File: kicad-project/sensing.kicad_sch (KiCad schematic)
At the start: 10 parts, among them J7 Screw_Terminal_01x04

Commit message: commit anonimo di thimas
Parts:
- added TP4, TP5: TestPoint, TestPoint:TestPoint_Keystone_5005-5009_Compact, symbol Connector:TestPoint
- gave numbers to parts that had none: 1
- renumbered D6 to D8, J7 to J8, R22 to R21, R24 to R22, R25 to R23
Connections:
- net Pan_V_Part: now also TP5.1
- net Shunt+: now also TP4.1
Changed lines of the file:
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@@
+    (stroke (width 0) (type default) (color 0 0 0 0))
+  )
+  (wire (pts (xy 99.06 97.79) (xy 111.76 97.79))
     (stroke (width 0) (type default) (color 0 0 0 0))
   )
@@
   )
   (wire (pts (xy 54.61 60.96) (xy 54.61 63.5))
+    (stroke (width 0) (type default) (color 0 0 0 0))
+  )
+  (wire (pts (xy 99.06 86.36) (xy 107.95 86.36))
     (stroke (width 0) (type default) (color 0 0 0 0))
   )
@@
     (effects (font (size 1.27 1.27)) (justify left bottom))
   )
+  (label "Shunt+" (at 99.06 86.36 0)
+    (effects (font (size 1.27 1.27)) (justify left bottom))
+  )
   (label "Pan_V_Part" (at 109.22 52.07 0)
     (effects (font (size 1.27 1.27)) (justify left bottom))
   )
   (label "Panel OUT -" (at 38.1 95.25 0)
+    (effects (font (size 1.27 1.27)) (justify left bottom))
+  )
+  (label "Pan_V_Part" (at 99.06 97.79 0)
     (effects (font (size 1.27 1.27)) (justify left bottom))
   )
@@
   (symbol (lib_id "Device:Opamp_Dual") (at 129.54 54.61 0) (unit 2)
     (in_bom yes) (on_board yes) (fields_autoplaced)
-    (property "Reference" "U?" (id 0) (at 129.54 44.45 0))
+    (property "Reference" "U5" (id 0) (at 129.54 44.45 0))
     (property "Value" "LM2904B" (id 1) (at 129.54 46.99 0))
     (property "Footprint" "Package_SO:TSSOP-8_4.4x3mm_P0.65mm" (id 2) (at 129.54 54.61 0)
@@
   (symbol (lib_id "power:GND") (at 106.68 60.96 0) (unit 1)
     (in_bom yes) (on_board yes)
-    (property "Reference" "#PWR073" (id 0) (at 106.68 67.31 0)
+    (property "Reference" "#PWR081" (id 0) (at 106.68 67.31 0)
       (effects (font (size 1.27 1.27)) hide)
     )
@@
   (symbol (lib_id "power:+3V3") (at 138.43 36.83 0) (unit 1)
     (in_bom yes) (on_board yes)
-    (property "Reference" "#PWR069" (id 0) (at 138.43 40.64 0)
+    (property "Reference" "#PWR082" (id 0) (at 138.43 40.64 0)
       (effects (font (size 1.27 1.27)) hide)
     )
@@
   (symbol (lib_id "power:GND") (at 59.69 54.61 0) (unit 1)
     (in_bom yes) (on_board yes)
-    (property "Reference" "#PWR?" (id 0) (at 59.69 60.96 0)
+    (property "Reference" "#PWR079" (id 0) (at 59.69 60.96 0)
       (effects (font (size 1.27 1.27)) hide)
     )
@@
   (symbol (lib_id "power:GND") (at 54.61 63.5 0) (unit 1)
     (in_bom yes) (on_board yes)
-    (property "Reference" "#PWR071" (id 0) (at 54.61 69.85 0)
+    (property "Reference" "#PWR078" (id 0) (at 54.61 69.85 0)
       (effects (font (size 1.27 1.27)) hide)
     )
@@
   (symbol (lib_id "Device:R") (at 106.68 57.15 0) (unit 1)
     (in_bom yes) (on_board yes) (fields_autoplaced)
-    (property "Reference" "R25" (id 0) (at 108.585 55.8799 0)
+    (property "Reference" "R23" (id 0) (at 108.585 55.8799 0)
       (effects (font (size 1.27 1.27)) (justify left))
     )
@@
   (symbol (lib_id "Device:Opamp_Dual") (at 67.31 52.07 0) (unit 1)
     (in_bom yes) (on_board yes) (fields_autoplaced)
-    (property "Reference" "U?" (id 0) (at 67.31 41.91 0))
+    (property "Reference" "U5" (id 0) (at 67.31 41.91 0))
     (property "Value" "LM2904B" (id 1) (at 67.31 44.45 0))
     (property "Footprint" "Package_SO:TSSOP-8_4.4x3mm_P0.65mm" (id 2) (at 67.31 52.07 0)
@@
     (pin "3")
   )
+  (symbol (lib_id "Connector:TestPoint") (at 107.95 86.36 0) (unit 1)
+    (in_bom yes) (on_board yes) (fields_autoplaced)
+    (property "Reference" "TP4" (id 0) (at 110.49 81.7879 0)
+      (effects (font (size 1.27 1.27)) (justify left))
+    )
+    (property "Value" "TestPoint" (id 1) (at 110.49 84.3279 0)
+      (effects (font (size 1.27 1.27)) (justify left))
+    )
+    (property "Footprint" "TestPoint:TestPoint_Keystone_5005-5009_Compact" (id 2) (at 113.03 86.36 0)
+      (effects (font (size 1.27 1.27)) hide)
+    )
+    (property "Datasheet" "~" (id 3) (at 113.03 86.36 0)
+      (effects (font (size 1.27 1.27)) hide)
+    )
+    (pin "1")
+  )
+  (symbol (lib_id "Connector:TestPoint") (at 111.76 97.79 0) (unit 1)
+    (in_bom yes) (on_board yes) (fields_autoplaced)
+    (property "Reference" "TP5" (id 0) (at 114.3 93.2179 0)
+      (effects (font (size 1.27 1.27)) (justify left))
+    )
+    (property "Value" "TestPoint" (id 1) (at 114.3 95.7579 0)
+      (effects (font (size 1.27 1.27)) (justify left))
+    )
+    (property "Footprint" "TestPoint:TestPoint_Keystone_5005-5009_Compact" (id 2) (at 116.84 97.79 0)
+      (effects (font (size 1.27 1.27)) hide)
+    )
+    (property "Datasheet" "~" (id 3) (at 116.84 97.79 0)
+      (effects (font (size 1.27 1.27)) hide)
+    )
+    (pin "1")
+  )
   (symbol (lib_id "Device:R") (at 106.68 46.99 0) (unit 1)
     (in_bom yes) (on_board yes) (fields_autoplaced)
-    (property "Reference" "R24" (id 0) (at 108.585 45.7199 0)
+    (property "Reference" "R22" (id 0) (at 108.585 45.7199 0)
       (effects (font (size 1.27 1.27)) (justify left))
     )
@@
   (symbol (lib_id "Device:Opamp_Dual") (at 148.59 34.29 90) (unit 3)
     (in_bom yes) (on_board yes) (fields_autoplaced)
-    (property "Reference" "U?" (id 0) (at 148.59 31.75 90))
+    (property "Reference" "U5" (id 0) (at 148.59 31.75 90))
     (property "Value" "LM2904B" (id 1) (at 148.59 34.29 90))
     (property "Footprint" "Package_SO:TSSOP-8_4.4x3mm_P0.65mm" (id 2) (at 148.59 34.29 0)
@@
   (symbol (lib_id "Device:R") (at 54.61 57.15 180) (unit 1)
     (in_bom yes) (on_board yes)
-    (property "Reference" "R22" (id 0) (at 50.8 58.42 0))
+    (property "Reference" "R21" (id 0) (at 50.8 58.42 0))
     (property "Value" "R" (id 1) (at 52.07 55.88 0))
     (property "Footprint" "Resistor_SMD:R_0603_1608Metric" (id 2) (at 56.388 57.15 90)
@@
   (symbol (lib_id "power:GND") (at 24.13 69.85 0) (unit 1)
     (in_bom yes) (on_board yes)
-    (property "Reference" "#PWR068" (id 0) (at 24.13 76.2 0)
+    (property "Reference" "#PWR076" (id 0) (at 24.13 76.2 0)
       (effects (font (size 1.27 1.27)) hide)
     )
@@
   (symbol (lib_id "power:GND") (at 27.94 54.61 0) (unit 1)
     (in_bom yes) (on_board yes)
-    (property "Reference" "#PWR?" (id 0) (at 27.94 60.96 0)
+    (property "Reference" "#PWR077" (id 0) (at 27.94 60.96 0)
       (effects (font (size 1.27 1.27)) hide)
     )
@@
   (symbol (lib_id "Connector:Screw_Terminal_01x04") (at 57.15 100.33 0) (mirror x) (unit 1)
     (in_bom yes) (on_board yes) (fields_autoplaced)
-    (property "Reference" "J7" (id 0) (at 57.15 88.9 0))
+    (property "Reference" "J8" (id 0) (at 57.15 88.9 0))
     (property "Value" "Screw_Terminal_01x04" (id 1) (at 57.15 91.44 0))
     (property "Footprint" "TerminalBlock_TE-Connectivity:TerminalBlock_TE_282834-4_1x04_P2.54mm_Horizontal" (id 2) (at 57.15 100.33 0)
@@
   (symbol (lib_id "power:GND") (at 158.75 36.83 0) (unit 1)
     (in_bom yes) (on_board yes)
-    (property "Reference" "#PWR070" (id 0) (at 158.75 43.18 0)
+    (property "Reference" "#PWR083" (id 0) (at 158.75 43.18 0)
       (effects (font (size 1.27 1.27)) hide)
     )
@@
   (symbol (lib_id "Device:D_Zener") (at 95.25 57.15 270) (unit 1)
     (in_bom yes) (on_board yes) (fields_autoplaced)
-    (property "Reference" "D6" (id 0) (at 97.79 55.8799 90)
+    (property "Reference" "D8" (id 0) (at 97.79 55.8799 90)
       (effects (font (size 1.27 1.27)) (justify left))
     )
@@
   (symbol (lib_id "power:GND") (at 95.25 60.96 0) (unit 1)
     (in_bom yes) (on_board yes)
-    (property "Reference" "#PWR072" (id 0) (at 95.25 67.31 0)
-      (effects (font (size 1.27 1.27)) hide)
-    )
+    (property "Reference" "#PWR080" (id 0) (at 95.25 67.31 0)
+      (effects (font (size 1.27 1.27)) hide)
+    )

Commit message: hw: add mounting holes
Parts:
- renumbered R19 to R21, R20 to R22, R21 to R23, R22 to R24, R23 to R25
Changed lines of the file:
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@@
   (symbol (lib_id "Device:R") (at 106.68 57.15 0) (unit 1)
     (in_bom yes) (on_board yes) (fields_autoplaced)
-    (property "Reference" "R23" (id 0) (at 108.585 55.8799 0)
+    (property "Reference" "R25" (id 0) (at 108.585 55.8799 0)
       (effects (font (size 1.27 1.27)) (justify left))
     )
@@
   (symbol (lib_id "Device:R") (at 106.68 46.99 0) (unit 1)
     (in_bom yes) (on_board yes) (fields_autoplaced)
-    (property "Reference" "R22" (id 0) (at 108.585 45.7199 0)
+    (property "Reference" "R24" (id 0) (at 108.585 45.7199 0)
       (effects (font (size 1.27 1.27)) (justify left))
     )
@@
   (symbol (lib_id "Device:R") (at 54.61 57.15 180) (unit 1)
     (in_bom yes) (on_board yes)
-    (property "Reference" "R21" (id 0) (at 50.8 58.42 0))
+    (property "Reference" "R23" (id 0) (at 50.8 58.42 0))
     (property "Value" "R" (id 1) (at 52.07 55.88 0))
     (property "Footprint" "Resistor_SMD:R_0603_1608Metric" (id 2) (at 56.388 57.15 90)
@@
   (symbol (lib_id "Device:R") (at 40.64 49.53 90) (unit 1)
     (in_bom yes) (on_board yes)
-    (property "Reference" "R20" (id 0) (at 40.64 44.45 90))
+    (property "Reference" "R22" (id 0) (at 40.64 44.45 90))
     (property "Value" "R" (id 1) (at 40.64 46.99 90))
     (property "Footprint" "Resistor_SMD:R_0603_1608Metric" (id 2) (at 40.64 51.308 90)
@@
   (symbol (lib_id "Device:R_Shunt") (at 24.13 52.07 0) (unit 1)
     (in_bom yes) (on_board yes) (fields_autoplaced)
-    (property "Reference" "R19" (id 0) (at 22.225 50.7999 0)
+    (property "Reference" "R21" (id 0) (at 22.225 50.7999 0)
       (effects (font (size 1.27 1.27)) (justify right))
     )

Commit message: hw: first layout draft
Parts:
- removed R21: R_Shunt, Resistor_SMD:R_1210_3225Metric, symbol Device:R_Shunt
- added R21: R_Shunt, Resistor_SMD:R_1210_3225Metric, symbol Device:R
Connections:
- net Shunt+ is gone; now on net Panel IN -: R22.1, TP4.1
- net GND: now also R21.2
- net Panel IN -: now also R21.1
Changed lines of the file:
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@@
   (junction (at 54.61 49.53) (diameter 0) (color 0 0 0 0)
   )
+  (junction (at 24.13 49.53) (diameter 0) (color 0 0 0 0)
+  )
   (junction (at 138.43 54.61) (diameter 0) (color 0 0 0 0)
   )
@@
     (stroke (width 0) (type default) (color 0 0 0 0))
   )
-  (wire (pts (xy 24.13 46.99) (xy 24.13 35.56))
+  (wire (pts (xy 24.13 35.56) (xy 24.13 49.53))
     (stroke (width 0) (type default) (color 0 0 0 0))
   )
@@
     (stroke (width 0) (type default) (color 0 0 0 0))
   )
-  (wire (pts (xy 27.94 49.53) (xy 36.83 49.53))
+  (wire (pts (xy 24.13 49.53) (xy 36.83 49.53))
     (stroke (width 0) (type default) (color 0 0 0 0))
   )
@@
     (pin "8")
   )
+  (symbol (lib_id "Device:R") (at 24.13 53.34 0) (unit 1)
+    (in_bom yes) (on_board yes) (fields_autoplaced)
+    (property "Reference" "R21" (id 0) (at 26.67 52.0699 0)
+      (effects (font (size 1.27 1.27)) (justify left))
+    )
+    (property "Value" "R_Shunt" (id 1) (at 26.67 54.6099 0)
+      (effects (font (size 1.27 1.27)) (justify left))
+    )
+    (property "Footprint" "Resistor_SMD:R_1210_3225Metric" (id 2) (at 22.352 53.34 90)
+      (effects (font (size 1.27 1.27)) hide)
+    )
+    (property "Datasheet" "~" (id 3) (at 24.13 53.34 0)
+      (effects (font (size 1.27 1.27)) hide)
+    )
+    (pin "1")
+    (pin "2")
+  )
   (symbol (lib_id "Device:R") (at 54.61 57.15 180) (unit 1)
     (in_bom yes) (on_board yes)
@@
     (pin "1")
   )
-  (symbol (lib_id "power:GND") (at 27.94 54.61 0) (unit 1)
-    (in_bom yes) (on_board yes)
-    (property "Reference" "#PWR077" (id 0) (at 27.94 60.96 0)
-      (effects (font (size 1.27 1.27)) hide)
-    )
-    (property "Value" "GND" (id 1) (at 27.94 58.42 0))
-    (property "Footprint" "" (id 2) (at 27.94 54.61 0)
-      (effects (font (size 1.27 1.27)) hide)
-    )
-    (property "Datasheet" "" (id 3) (at 27.94 54.61 0)
-      (effects (font (size 1.27 1.27)) hide)
-    )
-    (pin "1")
-  )
   (symbol (lib_id "Device:R") (at 40.64 49.53 90) (unit 1)
     (in_bom yes) (on_board yes)
@@
     (pin "2")
   )
-  (symbol (lib_id "Device:R_Shunt") (at 24.13 52.07 0) (unit 1)
-    (in_bom yes) (on_board yes) (fields_autoplaced)
-    (property "Reference" "R21" (id 0) (at 22.225 50.7999 0)
-      (effects (font (size 1.27 1.27)) (justify right))
-    )
-    (property "Value" "R_Shunt" (id 1) (at 22.225 53.3399 0)
-      (effects (font (size 1.27 1.27)) (justify right))
-    )
-    (property "Footprint" "Resistor_SMD:R_1210_3225Metric" (id 2) (at 22.352 52.07 90)
-      (effects (font (size 1.27 1.27)) hide)
-    )
-    (property "Datasheet" "~" (id 3) (at 24.13 52.07 0)
-      (effects (font (size 1.27 1.27)) hide)
-    )
-    (pin "1")
-    (pin "2")
-    (pin "3")
-    (pin "4")
-  )
   (symbol (lib_id "Connector:Screw_Terminal_01x04") (at 57.15 100.33 0) (mirror x) (unit 1)

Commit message: hw: classroom changes
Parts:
- removed U5: LM2904B, Package_SO:TSSOP-8_4.4x3mm_P0.65mm, symbol Device:Opamp_Dual
- added C26: C, Capacitor_SMD:C_0603_1608Metric, symbol Device:C
- R21: value R_Shunt -> 500m
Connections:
- net Pan_V_Part is gone; now on net V_{PANEL}: D8.1 (K), R24.2, R25.1, TP5.1
- net GND: now also R23.2, C26.2; no longer R23.1
- net I_{PANEL}: now also R22.2, C26.1
- net V_{PANEL}: now also R23.1
- removed net Shunt_V+: R22.2, R23.2
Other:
- note added: "I_{SC}=500mA"
- note added: "V_{OC}=20V"

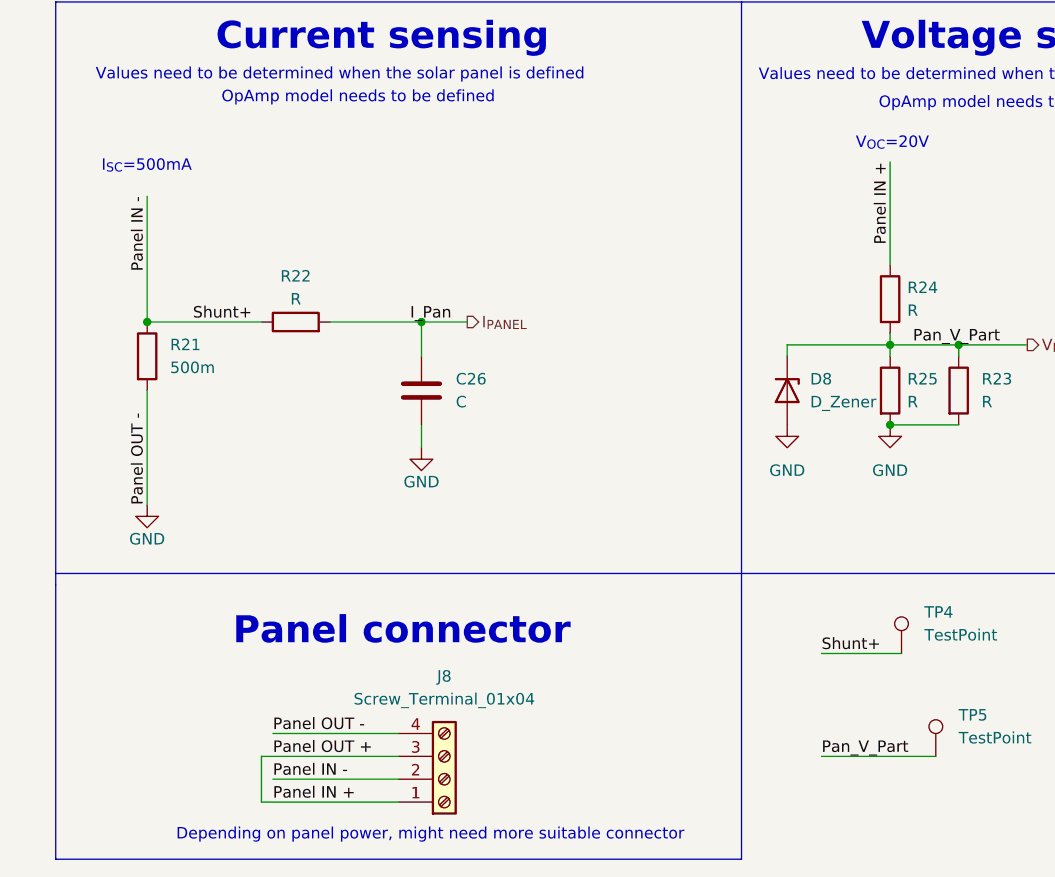
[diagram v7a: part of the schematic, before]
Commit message: change mcu pins and optimize layout
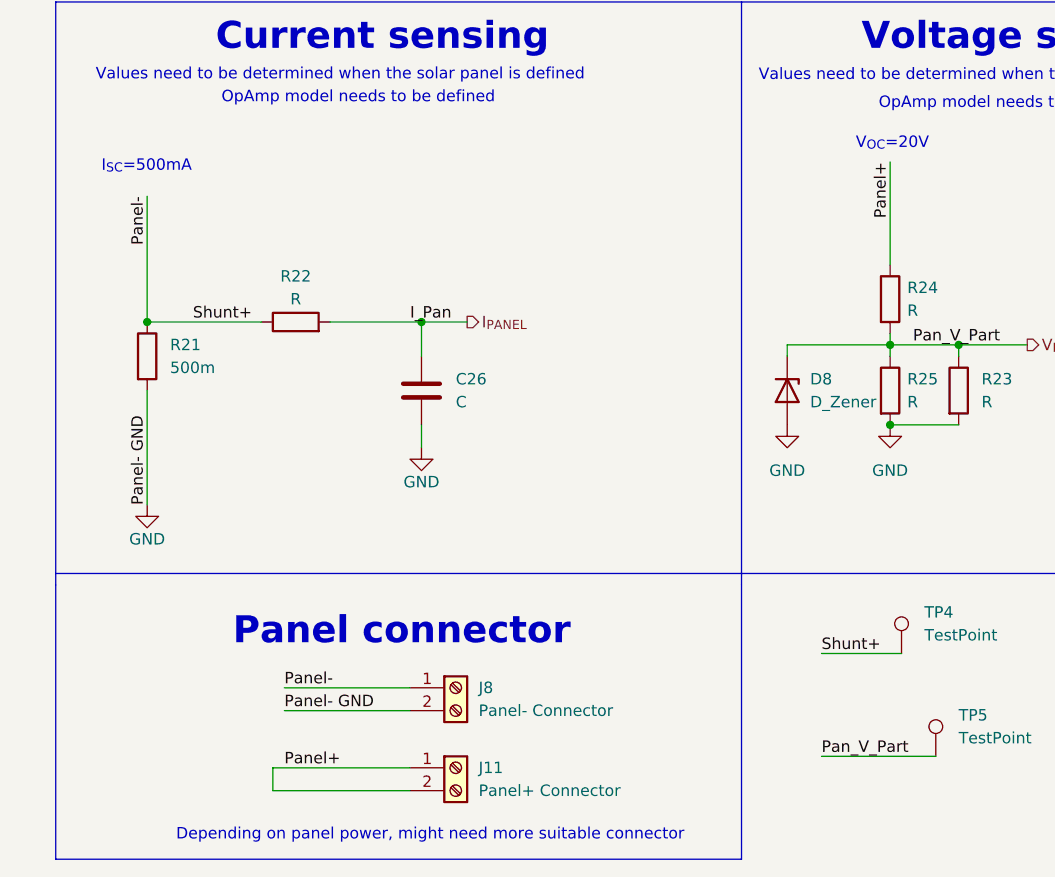
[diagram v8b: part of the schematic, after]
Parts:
- removed J8: Screw_Terminal_01x04, TerminalBlock_TE-Connectivity:TerminalBlock_TE_282834-4_1x04_P2.54mm_Horizontal, symbol Connector:Screw_Terminal_01x04
- added J11: Panel+ Connector, TerminalBlock_TE-Connectivity:TerminalBlock_TE_282834-2_1x02_P2.54mm_Horizontal, symbol Connector:Screw_Terminal_01x02
- added J8: Panel- Connector, TerminalBlock_TE-Connectivity:TerminalBlock_TE_282834-2_1x02_P2.54mm_Horizontal, symbol Connector:Screw_Terminal_01x02
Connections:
- net GND: now also J8.2 (Pin_2)
- net Panel IN + renamed Panel+
- net Panel+: now also J11.1 (Pin_1), J11.2 (Pin_2)
- net Panel IN - renamed Panel-
- net Panel-: now also J8.1 (Pin_1)
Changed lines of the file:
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@@
     (stroke (width 0) (type default) (color 0 0 0 0))
   )
-  (wire (pts (xy 52.07 97.79) (xy 36.83 97.79))
-    (stroke (width 0) (type default) (color 0 0 0 0))
-  )
-  (wire (pts (xy 52.07 100.33) (xy 38.1 100.33))
+  (wire (pts (xy 53.34 99.06) (xy 38.1 99.06))
+    (stroke (width 0) (type default) (color 0 0 0 0))
+  )
+  (wire (pts (xy 53.34 92.71) (xy 39.37 92.71))
     (stroke (width 0) (type default) (color 0 0 0 0))
   )
@@
     (stroke (width 0) (type default) (color 0 0 0 0))
   )
-  (wire (pts (xy 52.07 95.25) (xy 38.1 95.25))
+  (wire (pts (xy 53.34 90.17) (xy 39.37 90.17))
     (stroke (width 0) (type default) (color 0 0 0 0))
   )
@@
     (stroke (width 0) (type default) (color 0 0 0 0))
   )
-  (wire (pts (xy 36.83 97.79) (xy 36.83 102.87))
+  (wire (pts (xy 38.1 99.06) (xy 38.1 101.6))
     (stroke (width 0) (type default) (color 0 0 0 0))
   )
@@
     (stroke (width 0) (type default) (color 0 0 0 0))
   )
-  (wire (pts (xy 52.07 102.87) (xy 36.83 102.87))
+  (wire (pts (xy 53.34 101.6) (xy 38.1 101.6))
     (stroke (width 0) (type default) (color 0 0 0 0))
   )
@@
     (effects (font (size 1.27 1.27)) (justify left bottom))
   )
-  (label "Panel OUT +" (at 38.1 97.79 0)
-    (effects (font (size 1.27 1.27)) (justify left bottom))
-  )
-  (label "Panel OUT -" (at 24.13 69.85 90)
-    (effects (font (size 1.27 1.27)) (justify left bottom))
-  )
-  (label "Panel IN -" (at 38.1 100.33 0)
-    (effects (font (size 1.27 1.27)) (justify left bottom))
-  )
-  (label "Panel IN +" (at 106.68 31.75 270)
+  (label "Panel- GND" (at 24.13 69.85 90)
+    (effects (font (size 1.27 1.27)) (justify left bottom))
+  )
+  (label "Panel-" (at 39.37 90.17 0)
+    (effects (font (size 1.27 1.27)) (justify left bottom))
+  )
+  (label "Panel+" (at 106.68 31.75 270)
     (effects (font (size 1.27 1.27)) (justify right bottom))
   )
@@
     (effects (font (size 1.27 1.27)) (justify left bottom))
   )
-  (label "Panel IN -" (at 24.13 35.56 270)
+  (label "Panel-" (at 24.13 35.56 270)
     (effects (font (size 1.27 1.27)) (justify right bottom))
   )
@@
     (effects (font (size 1.27 1.27)) (justify left bottom))
   )
-  (label "Panel OUT -" (at 38.1 95.25 0)
+  (label "Panel- GND" (at 39.37 92.71 0)
     (effects (font (size 1.27 1.27)) (justify left bottom))
   )
@@
     (effects (font (size 1.27 1.27)) (justify left bottom))
   )
-  (label "Panel IN +" (at 38.1 102.87 0)
+  (label "Panel+" (at 39.37 99.06 0)
     (effects (font (size 1.27 1.27)) (justify left bottom))
   )
@@
     )
     (pin "1")
+  )
+  (symbol (lib_id "Connector:Screw_Terminal_01x02") (at 58.42 99.06 0) (unit 1)
+    (in_bom yes) (on_board yes) (fields_autoplaced)
+    (property "Reference" "J11" (id 0) (at 60.96 99.0599 0)
+      (effects (font (size 1.27 1.27)) (justify left))
+    )
+    (property "Value" "Panel+ Connector" (id 1) (at 60.96 101.5999 0)
+      (effects (font (size 1.27 1.27)) (justify left))
+    )
+    (property "Footprint" "TerminalBlock_TE-Connectivity:TerminalBlock_TE_282834-2_1x02_P2.54mm_Horizontal" (id 2) (at 58.42 99.06 0)
+      (effects (font (size 1.27 1.27)) hide)
+    )
+    (property "Datasheet" "~" (id 3) (at 58.42 99.06 0)
+      (effects (font (size 1.27 1.27)) hide)
+    )
+    (pin "1")
+    (pin "2")
   )
   (symbol (lib_id "Device:R") (at 106.68 57.15 0) (unit 1)
@@
     (pin "2")
   )
-  (symbol (lib_id "Connector:Screw_Terminal_01x04") (at 57.15 100.33 0) (mirror x) (unit 1)
-    (in_bom yes) (on_board yes) (fields_autoplaced)
-    (property "Reference" "J8" (id 0) (at 57.15 88.9 0))
-    (property "Value" "Screw_Terminal_01x04" (id 1) (at 57.15 91.44 0))
-    (property "Footprint" "TerminalBlock_TE-Connectivity:TerminalBlock_TE_282834-4_1x04_P2.54mm_Horizontal" (id 2) (at 57.15 100.33 0)
-      (effects (font (size 1.27 1.27)) hide)
-    )
-    (property "Datasheet" "~" (id 3) (at 57.15 100.33 0)
-      (effects (font (size 1.27 1.27)) hide)
-    )
-    (pin "1")
-    (pin "2")
-    (pin "3")
-    (pin "4")
+  (symbol (lib_id "Connector:Screw_Terminal_01x02") (at 58.42 90.17 0) (unit 1)
+    (in_bom yes) (on_board yes) (fields_autoplaced)
+    (property "Reference" "J8" (id 0) (at 60.96 90.1699 0)
+      (effects (font (size 1.27 1.27)) (justify left))
+    )
+    (property "Value" "Panel- Connector" (id 1) (at 60.96 92.7099 0)
+      (effects (font (size 1.27 1.27)) (justify left))
+    )
+    (property "Footprint" "TerminalBlock_TE-Connectivity:TerminalBlock_TE_282834-2_1x02_P2.54mm_Horizontal" (id 2) (at 58.42 90.17 0)
+      (effects (font (size 1.27 1.27)) hide)
+    )
+    (property "Datasheet" "~" (id 3) (at 58.42 90.17 0)
+      (effects (font (size 1.27 1.27)) hide)
+    )
+    (pin "1")
+    (pin "2")
   )
   (symbol (lib_id "Device:D_Zener") (at 95.25 57.15 270) (unit 1)
